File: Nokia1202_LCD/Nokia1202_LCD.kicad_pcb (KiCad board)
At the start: 2 copper layers, 28.4 x 33 mm, 5 parts, among them P1 CONN_01X08

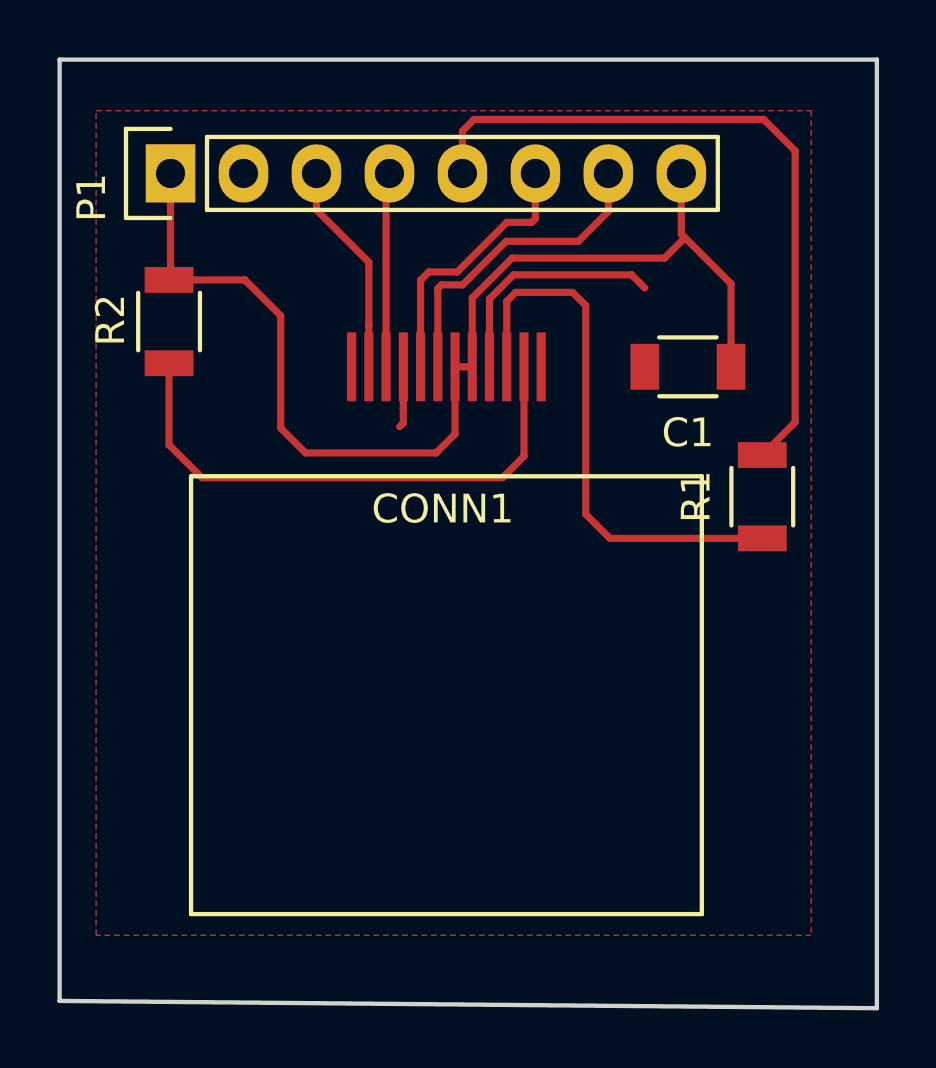
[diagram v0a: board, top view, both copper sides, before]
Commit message: Re-rout PCB for Nokia1202 LCD breakout board
Re-arrange the capacitor on vcc line and the 0ohm resistor on LED line
Re-route the signals
Add a bottom copper pour
Make the power routes thicker[0.4mm]
Resize the board smaller
Export schematic[PDF] and PCB layout[SVG] for prototyping
Export PNG image of the 3D view
Delete an unsed image of an LCD pinout
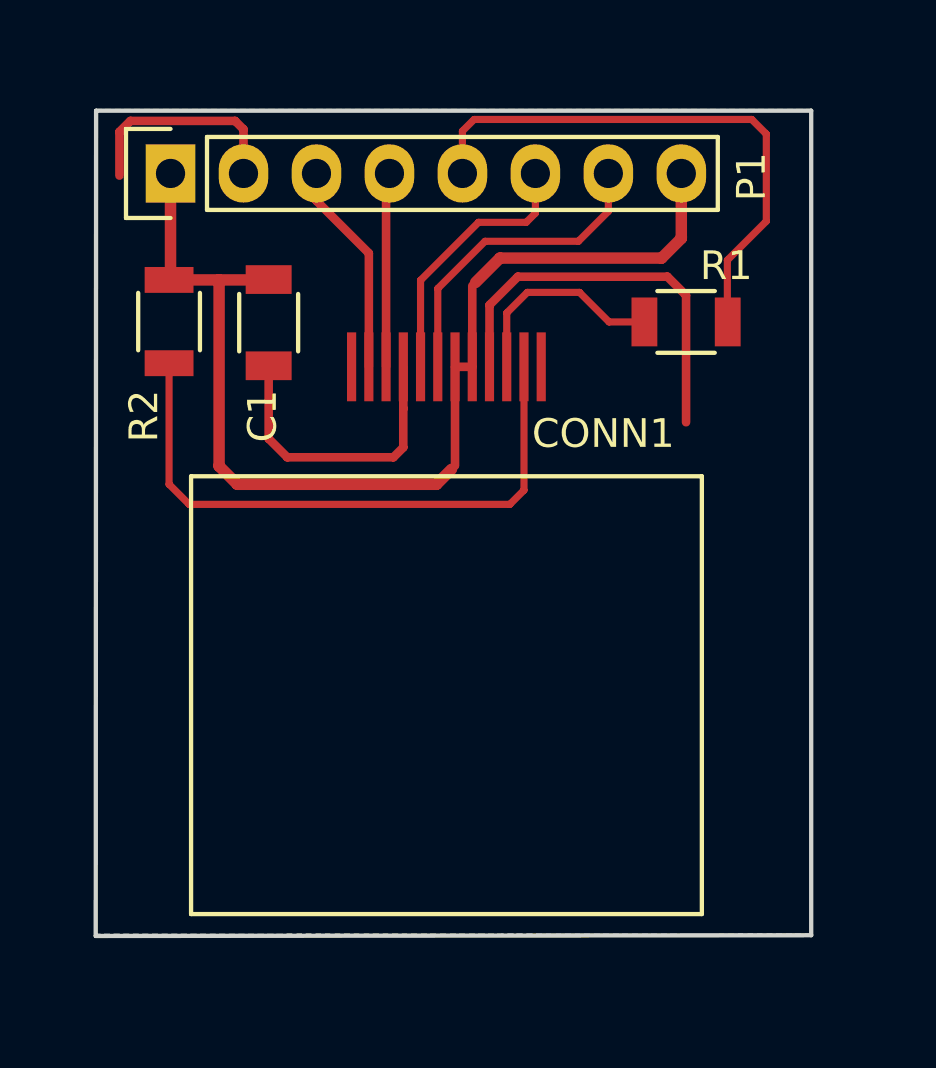
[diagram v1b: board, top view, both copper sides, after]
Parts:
- moved C1 14.7 mm to (123.9, 96.0), turned to 270 degrees
- moved R1 6.64 mm to (138.4, 96.0), turned to 0 degrees
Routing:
- net GND: track 10.4 -> 32.2 mm
- net Net-(CONN1-Pad10): track 19.1 -> 7.39 mm
- net LED: track 24.7 -> 19.5 mm
- net Net-(CONN1-Pad11): track 19.1 -> 21.4 mm
- added copper zone on B.Cu, net GND
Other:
- board size 28.4 x 33 mm -> 24.9 x 28.7 mm

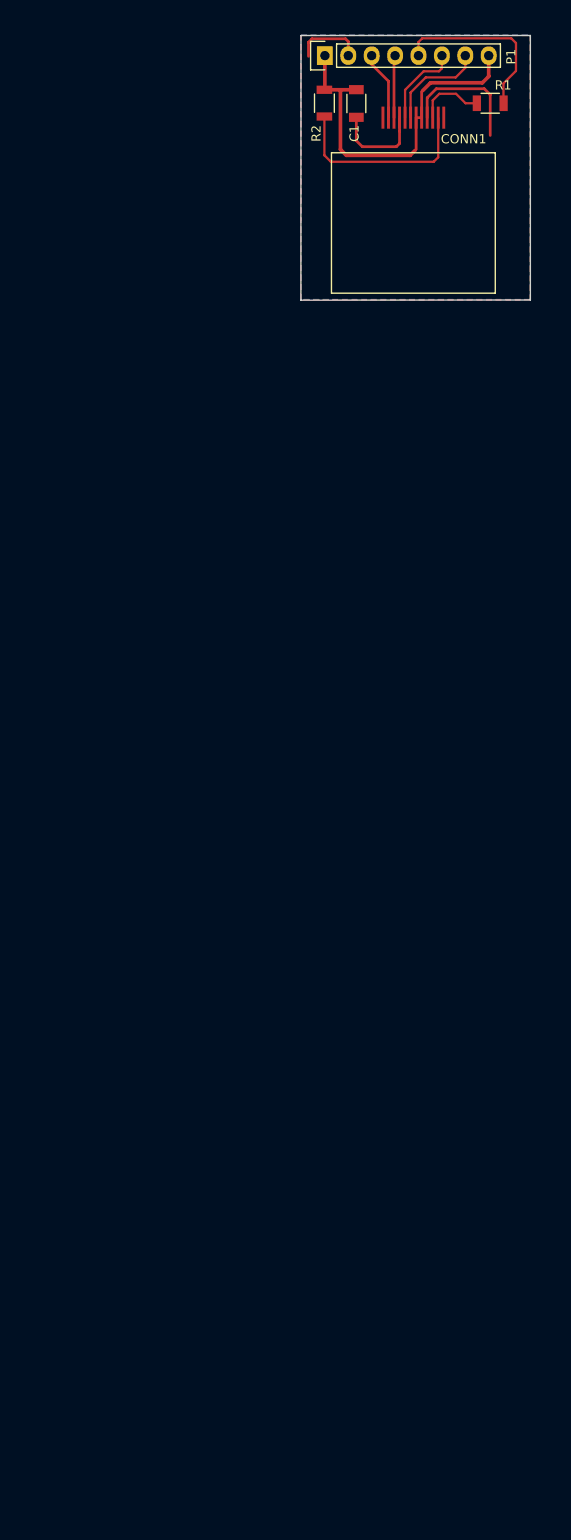
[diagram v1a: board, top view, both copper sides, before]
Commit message: Too many untracked changes: LCD boards update and switch to KiCAD version 5
Update the Nokia LCD breakout boards
Add more KiCAD simulation projects
Update most projects to KiCAD version 5
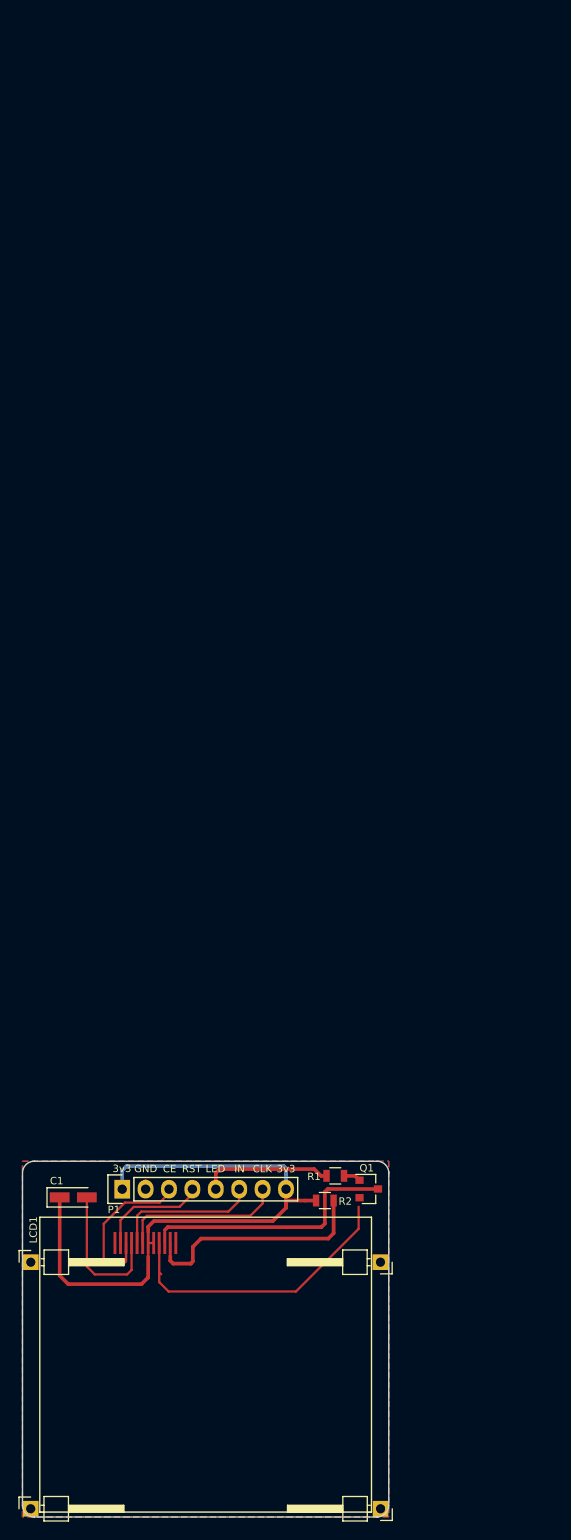
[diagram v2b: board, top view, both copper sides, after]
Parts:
- removed CONN1: nokia1202LCD, Connect:Nokia1202LCD
- added J1: Conn_01x01, Pin_Headers:Pin_Header_Angled_1x01_Pitch2.54mm, F.Cu at (88.5, 248.5)
- added J2: Conn_01x01, Pin_Headers:Pin_Header_Angled_1x01_Pitch2.54mm, F.Cu at (126.5, 248.5)
- added J3: Conn_01x01, Pin_Headers:Pin_Header_Angled_1x01_Pitch2.54mm, F.Cu at (88.5, 221.8)
- added J4: Conn_01x01, Pin_Headers:Pin_Header_Angled_1x01_Pitch2.54mm, F.Cu at (126.5, 221.8)
- added LCD1: Nokia1202_LCD, Displays:Nokia1202LCD_folded, F.Cu at (101.0, 219.7)
- added Q1: Q_NPN_BEC, TO_SOT_Packages_SMD:SOT-23, F.Cu at (125.2, 213.8)
- C1: value 0.1 -> 0.1u; footprint Capacitors_SMD:C_1206 -> Capacitors_Tantalum_SMD:CP_Tantalum_Case-A_EIA-3216-18_Wave
- R1: value 0 -> 1K; footprint Resistors_SMD:R_1206 -> Resistors_SMD:R_0805
- R2: footprint Resistors_SMD:R_1206 -> Resistors_SMD:R_0805
- moved P1 125.0 mm to (98.4, 213.9)
- moved C1 122.6 mm to (93.1, 214.7), turned to 0 degrees
- moved R2 119.1 mm to (120.4, 215.1), turned to 180 degrees
- moved R1 117.6 mm to (121.6, 212.4)
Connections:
- P1 pad 3: RESET -> CE
- P1 pad 4: CE -> RESET
- R1 pad 1: Net-(CONN1-Pad10) -> LED
- R1 pad 2: LED -> Net-(Q1-Pad1)
- R2 pad 1: VCC -> Net-(LCD1-Pad11)
- R2 pad 2: Net-(CONN1-Pad11) -> VCC
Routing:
- net VCC: track 39.5 -> 68.3 mm
- net LED-: track 0.00 -> 28.4 mm
- net Net-(LCD1-Pad11): track 0.00 -> 25.6 mm
- net Net-(CONN1-Pad11): track 21.4 -> 0.00 mm
- net GND: track 32.2 -> 47.5 mm
- net CE: track 6.78 -> 17.7 mm
- net Net-(CONN1-Pad10): track 7.39 -> 0.00 mm
- net CLK: track 11.1 -> 17.8 mm
- net MOSI: track 9.36 -> 16.0 mm
- net LED: track 19.5 -> 14.3 mm
- net RESET: track 7.49 -> 12.0 mm
- net Net-(Q1-Pad1): track 0.00 -> 1.88 mm
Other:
- board size 24.9 x 28.7 mm -> 39.8 x 38.6 mm
- rule pad_to_mask_clearance: 0.2 -> 0.04
- board text added: "3v3"
- board text added: "@muriukidavid http://karibe.co.ke"
- board text added: "CE"
- board text added: "CLK"
- board text added: "GND"
- board text added: "IN"
- board text added: "Karibe (K) Ltd"
- board text added: "LED"
- board text added: "RST"
